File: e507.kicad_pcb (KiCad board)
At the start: 4 copper layers, 25 x 84.8 mm, 83 parts, among them J1 GT-USB-7010ASV, J2 DM3CS-SF, J3 SJ-3523-SMT-TR, J4 SCREEN, P1 S2B-PH-SM4-TB, U1 BQ25185DLHR, U2 TPS73633DBVT, U3 TPS631000DRLR, U5 USBLC6-2SC6, U6 PCM5102APWR, U7 TPA6132A2RTER, U8 SiP32431DR3, U9 STM32F446RETx

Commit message: add clock
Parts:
- added C38: 22pF, Capacitor_SMD:C_0402_1005Metric, F.Cu at (63.8, 62.1)
- added C39: 22pF, Capacitor_SMD:C_0402_1005Metric, F.Cu at (60.2, 68.1)
- added Y1: X50328MSB2GI, Crystal:Crystal_SMD_5032-2Pin_5.0x3.2mm, F.Cu at (63.4, 66.2)
- moved R13 17.6 mm to (80.5, 65.8), turned to 90 degrees
- moved S1 16.1 mm to (79.5, 61.5)
- moved C10 15.8 mm to (76.8, 64.0), turned to 180 degrees
- moved C33 1.61 mm to (68.0, 65.2), turned to 90 degrees
- moved J4 1.50 mm to (67.7, 61.5)
- moved R16 0.75 mm to (60.0, 62.2), turned to -90 degrees
- moved C34 0.71 mm to (61.4, 69.7), turned to 135 degrees
- moved C15 0.57 mm to (73.5, 48.5), turned to 0 degrees
- moved C29 0.50 mm to (75.0, 47.1)
- moved C26 0.22 mm to (71.4, 46.4)
- moved C14 0.14 mm to (71.9, 48.0)
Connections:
- U9 pad 5: unconnected-(U9-PH0-Pad5) -> /MCU/OSC-
- U9 pad 6: unconnected-(U9-PH1-Pad6) -> /MCU/OSC+
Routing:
- net /MCU/IO_VOLUME_UP: track 23.0 -> 0.00 mm
- net /MCU/IO_RESET: track 6.91 -> 24.8 mm, vias 0 -> 2
- net /MCU/OSC-: track 0.00 -> 6.88 mm
- net /MCU/OSC+: track 0.00 -> 6.27 mm
- net GND: track 34.1 -> 31.5 mm, vias 40 -> 41
- net Net-(U6-CAPM): track 0.00 -> 2.13 mm
- net Net-(U6-CAPP): track 0.00 -> 1.91 mm
- net Net-(J3-RING): track 11.9 -> 13.6 mm
- net +3V3: track 172.2 -> 170.9 mm
- net /Audio/IO_DAC_DIN: track 17.6 -> 18.7 mm

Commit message: some fixes
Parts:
- removed R14: 10K, Resistor_SMD:R_0402_1005Metric
- moved R16 18.5 mm to (77.0, 69.5), turned to 0 degrees
- moved R7 7.42 mm to (77.0, 71.5), turned to -45 degrees
- moved R17 5.72 mm to (76.5, 68.5)
- moved R21 5.14 mm to (77.2, 76.8), turned to 45 degrees
- moved S2 0.50 mm to (76.5, 66.2)
- moved C11 0.20 mm to (76.6, 75.9)
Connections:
- J1 pad A6: /Power/USB_D+ -> /Power/USB_DP
- J1 pad A7: /Power/USB_D- -> /Power/USB_DN
- J1 pad B6: /Power/USB_D+ -> /Power/USB_DP
- J1 pad B7: /Power/USB_D- -> /Power/USB_DN
- U5 pad 1: /Power/USB_D- -> /Power/USB_DN
- U5 pad 3: /Power/USB_D+ -> /Power/USB_DP
- U5 pad 4: /Power/USB_D+ -> /MCU/USB_D+
- U5 pad 6: /Power/USB_D- -> /MCU/USB_D-
- U9 pad 44: /Power/USB_D- -> /MCU/USB_D-
- U9 pad 45: /Power/USB_D+ -> /MCU/USB_D+
- U9 pad 46: unconnected-(U9-PA13-Pad46) -> /MCU/IO_CHG_STAT1
- U9 pad 51: unconnected-(U9-PC10-Pad51) -> /MCU/IO_CHG_STAT2
- U9 pad 52: unconnected-(U9-PC11-Pad52) -> /MCU/IO_BAT_V
- U9 pad 56: unconnected-(U9-PB4-Pad56) -> /MCU/IO_VOLUME_UP
- U9 pad 57: unconnected-(U9-PB5-Pad57) -> /MCU/IO_VOLUME_DOWN
- U9 pad 58: unconnected-(U9-PB6-Pad58) -> /MCU/IO_I2C_SCL
- U9 pad 59: unconnected-(U9-PB7-Pad59) -> /MCU/IO_I2C_SDA
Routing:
- net /MCU/IO_VOLUME_UP: track 0.00 -> 38.9 mm, vias 0 -> 2
- net /Power/USB_D+: track 38.9 -> 0.00 mm
- net /Power/USB_D-: track 38.6 -> 0.00 mm
- net /MCU/USB_D+: track 0.00 -> 33.0 mm
- net /MCU/USB_D-: track 0.00 -> 32.6 mm
- net /MCU/IO_I2C_SCL: track 0.00 -> 11.8 mm, vias 0 -> 1
- net /MCU/IO_I2C_SDA: track 0.00 -> 10.3 mm
- net /MCU/IO_BAT_V: track 18.6 -> 27.9 mm
- net /MCU/IO_CHG_STAT2: track 35.6 -> 44.7 mm
- net /Power/USB_DN: track 0.00 -> 6.01 mm
- net /Power/USB_DP: track 0.00 -> 5.94 mm
- net /MCU/IO_VOLUME_DOWN: track 33.2 -> 38.0 mm
- net +3V3: track 170.9 -> 167.1 mm
- net /MCU/IO_CHG_STAT1: track 38.7 -> 41.5 mm
- net GND: track 31.5 -> 34.0 mm, vias 41 -> 42
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
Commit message: todo list
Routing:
- net GND: track 34.0 -> 37.1 mm, vias 42 -> 43
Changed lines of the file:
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@@
-	)
-	(segment
-		(start 82.5625 93.76)
-		(end 81.17 93.76)
-		(width 0.6)
-		(layer "F.Cu")
-		(net "GND")
 	)
 	(segment
@@
 	)
 	(segment
-		(start 74.67 110.66)
-		(end 75.37 109.96)
-		(width 0.6)
-		(layer "F.Cu")
-		(net "GND")
-	)
-	(segment
 		(start 66.660589 81.339411)
 		(end 66.396055 81.074877)
@@
 		(end 60.553797 68.429402)
 		(width 0.2)
+		(layer "F.Cu")
+		(net "GND")
+	)
+	(segment
+		(start 74.67 110.66)
+		(end 74.67 111.407297)
+		(width 0.6)
 		(layer "F.Cu")
 		(net "GND")
@@
 	)
 	(segment
+		(start 76 108.59)
+		(end 75.38 109.21)
+		(width 0.6)
+		(layer "F.Cu")
+		(net "GND")
+	)
+	(segment
 		(start 60.910589 76.160589)
 		(end 61.467555 76.160589)
@@
 	)
 	(segment
+		(start 75.38 109.95)
+		(end 74.67 110.66)
+		(width 0.6)
+		(layer "F.Cu")
+		(net "GND")
+	)
+	(segment
+		(start 68.36 108.96)
+		(end 68.195 109.125)
+		(width 0.6)
+		(layer "F.Cu")
+		(net "GND")
+	)
+	(segment
 		(start 66.396055 80.424477)
 		(end 66.966979 79.853553)
@@
 		(end 62.370785 75.257359)
 		(width 0.2)
+		(layer "F.Cu")
+		(net "GND")
+	)
+	(segment
+		(start 76 108.25)
+		(end 76 108.59)
+		(width 0.6)
 		(layer "F.Cu")
 		(net "GND")
@@
 	)
 	(segment
+		(start 68.195 111.332297)
+		(end 68.27 111.407297)
+		(width 0.6)
+		(layer "F.Cu")
+		(net "GND")
+	)
+	(segment
 		(start 67.930213 78.896169)
 		(end 67.924363 78.896169)
@@
 	)
 	(segment
+		(start 68.195 109.125)
+		(end 68.195 111.332297)
+		(width 0.6)
+		(layer "F.Cu")
+		(net "GND")
+	)
+	(segment
 		(start 65.906319 78.792893)
 		(end 65.199212 79.5)
@@
 	)
 	(segment
+		(start 75.38 109.21)
+		(end 75.38 109.95)
+		(width 0.6)
+		(layer "F.Cu")
+		(net "GND")
+	)
+	(segment
 		(start 75.151936 103.55)
 		(end 75.351936 103.75)
@@
 	)
 	(segment
-		(start 81.17 93.76)
-		(end 81.12 93.71)
-		(width 0.6)
-		(layer "F.Cu")
-		(net "GND")
-	)
-	(segment
-		(start 74.67 111.407297)
-		(end 74.67 110.66)
-		(width 0.6)
-		(layer "F.Cu")
-		(net "GND")
-	)
-	(segment
 		(start 66.660589 82.339411)
 		(end 66.660589 81.339411)
@@
 		(net "GND")
 	)
+	(via
+		(at 64.72159 61.080507)
+		(size 0.6)
+		(drill 0.3)
+		(layers "F.Cu" "B.Cu")
+		(free yes)
+		(net "GND")
+	)

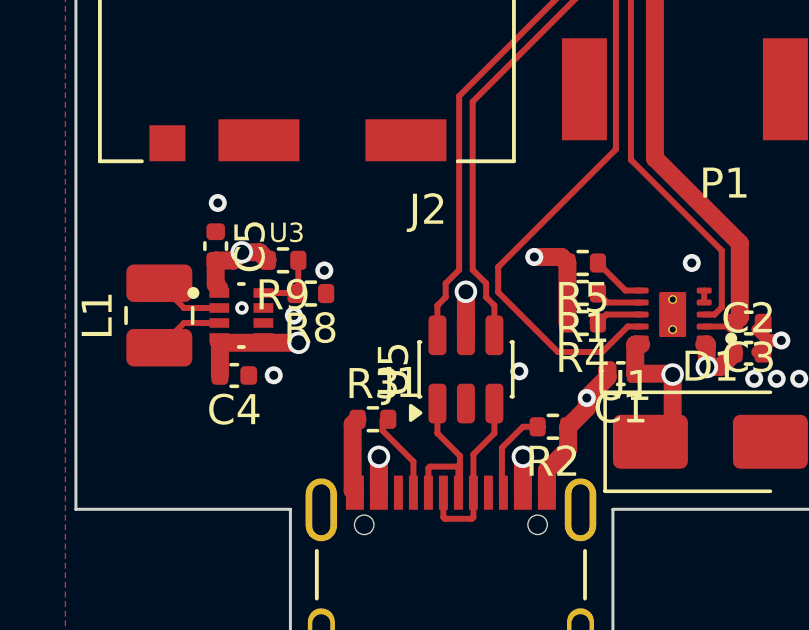
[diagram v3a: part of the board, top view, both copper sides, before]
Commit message: add mpns to buck boost
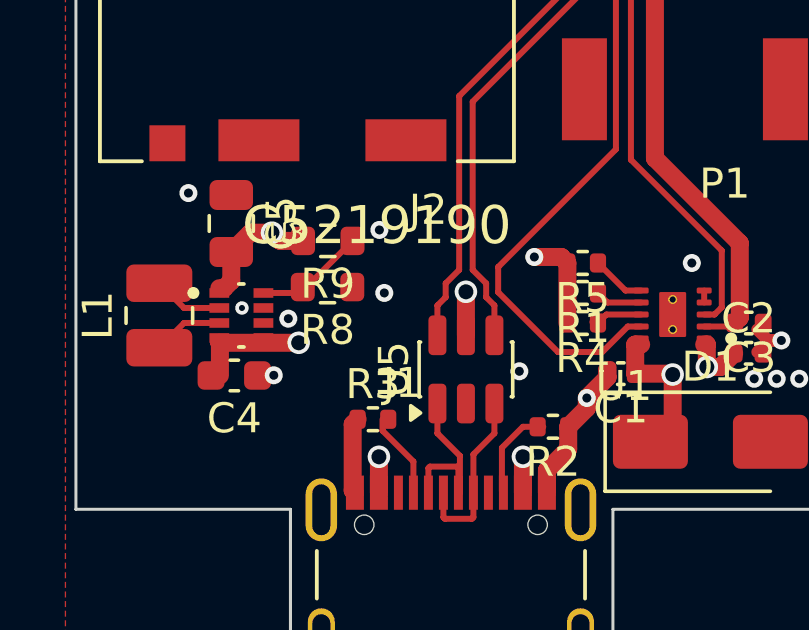
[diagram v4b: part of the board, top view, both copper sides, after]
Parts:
- C4: footprint Capacitor_SMD:C_0402_1005Metric -> Capacitor_SMD:C_0603_1608Metric
- C5: footprint Capacitor_SMD:C_0402_1005Metric -> Capacitor_SMD:C_0805_2012Metric
- R8: footprint Resistor_SMD:R_0402_1005Metric -> Resistor_SMD:R_0603_1608Metric
- R9: value 511K -> 510K; footprint Resistor_SMD:R_0402_1005Metric -> Resistor_SMD:R_0603_1608Metric
- moved R9 1.63 mm to (67.4, 103.0)
- moved C5 0.92 mm to (64.1, 102.4)
- moved R8 0.60 mm to (67.4, 104.6)
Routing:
- net Net-(U3-FB): track 2.18 -> 3.69 mm
- net +3V3: track 167.1 -> 168.2 mm
- net GND: vias 43 -> 44
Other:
- board text added: "C5219190"

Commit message: fill more parts
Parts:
- moved R21 14.2 mm to (63.2, 79.1), turned to 180 degrees
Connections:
- U9 pad 14: unconnected-(U9-PA0-Pad14) -> /MCU/IO_PLAY_POWER
- U9 pad 23: unconnected-(U9-PA7-Pad23) -> /MCU/IO_BAT_V
- U9 pad 24: unconnected-(U9-PC4-Pad24) -> /MCU/IO_CHG_STAT1
- U9 pad 46: /MCU/IO_CHG_STAT1 -> unconnected-(U9-PA13-Pad46)
- U9 pad 52: /MCU/IO_BAT_V -> unconnected-(U9-PC11-Pad52)
- U9 pad 56: /MCU/IO_VOLUME_UP -> unconnected-(U9-PB4-Pad56)
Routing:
- net GND: track 37.1 -> 40.9 mm, vias 44 -> 45
- net /MCU/IO_CHG_STAT1: track 41.5 -> 38.1 mm, vias 0 -> 2
- net /MCU/IO_PLAY_POWER: track 0.00 -> 1.45 mm, vias 0 -> 1
- net /MCU/IO_CHG_STAT2: track 44.7 -> 43.2 mm
- net /MCU/IO_BAT_V: track 27.9 -> 26.5 mm, vias 0 -> 2
- net +3V3: track 168.2 -> 169.1 mm

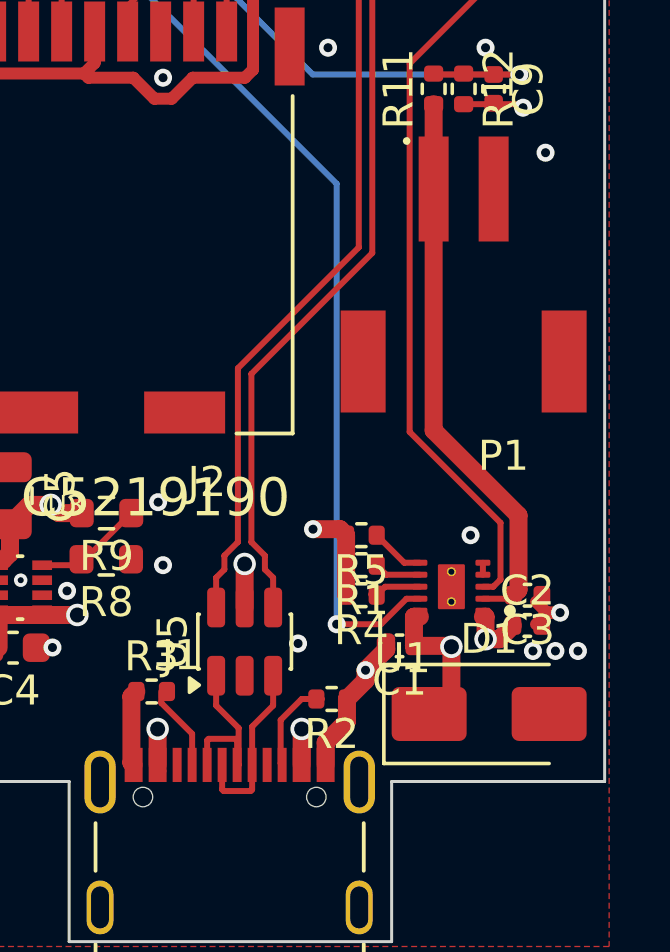
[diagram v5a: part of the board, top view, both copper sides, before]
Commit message: Finish all power MPNs
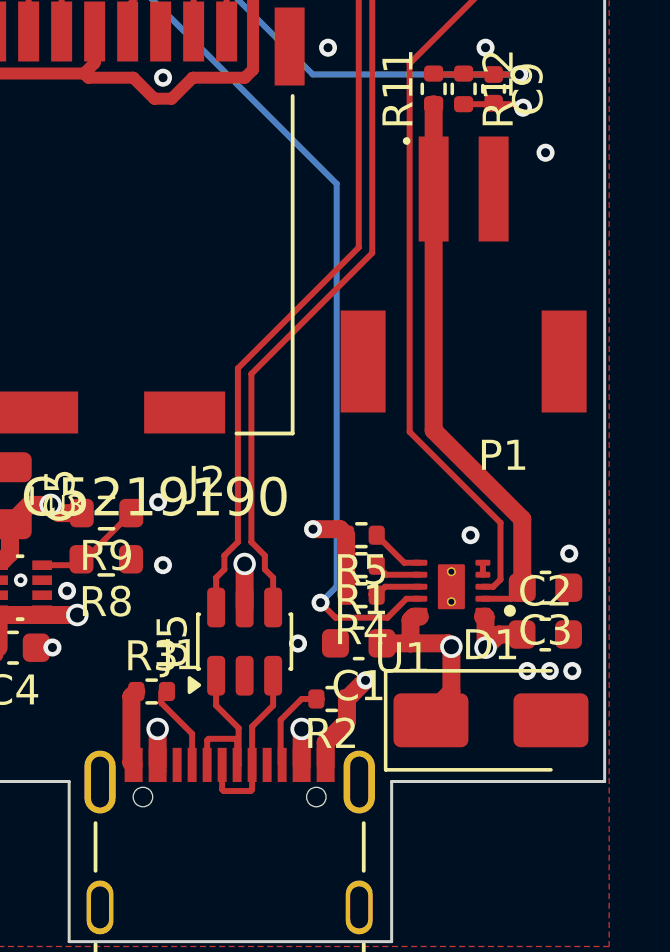
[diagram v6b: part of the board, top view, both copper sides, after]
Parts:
- C1, C2, C3: footprint Capacitor_SMD:C_0402_1005Metric -> Capacitor_SMD:C_0603_1608Metric
- moved C1 1.36 mm to (75.8, 107.4)
- moved C2 0.67 mm to (82.0, 107.1)
- moved C3 0.65 mm to (82.0, 105.5)
- moved D1 0.22 mm to (80.2, 109.9)
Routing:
- net GND: track 40.9 -> 37.3 mm
- net VBUS: track 9.37 -> 10.4 mm
- net VSYS: track 87.1 -> 87.9 mm
